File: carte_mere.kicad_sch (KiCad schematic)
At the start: 58 parts, among them J1 Conn_01x02_Pin, J10 Conn_01x03_Pin, J11 Conn_01x03_Pin, J12 Conn_01x03_Pin, J13 Conn_01x03_Pin, J14 Conn_01x03_Pin, J15 Conn_01x03_Pin, J16 Conn_01x03_Pin, J2 Conn_01x03_Pin, J3 Conn_01x03_Pin, J4 Conn_01x03_Pin, J5 Conn_01x03_Pin, J6 Conn_01x03_Pin, J7 Conn_01x03_Pin, J8 Conn_01x03_Pin, J9 Conn_01x03_Pin, U1 SN65HVD230, U2 SN74LVC1T45DBV

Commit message: update schematic
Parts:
- added C1, C2: 22uF, Capacitor_SMD:CP_Elec_5x5.4, symbol Device:CP_Small
- added D3, D4: D_Small, Diode_SMD:D_SMA_Handsoldering, symbol Device:D_Small
- added H1, H2, H3, H4: MountingHole_Pad_MP, MountingHole:MountingHole_3.2mm_M3_DIN965_Pad_TopBottom, symbol Mechanical:MountingHole_Pad_MP
- added J17, J18, J19: Conn_01x05_Pin, symbol Connector:Conn_01x05_Pin
- added J20, J21, J22, J23, J24: Conn_01x02_Pin, symbol Connector:Conn_01x02_Pin
- added R38, R40: 1k, symbol Device:R
- added R39, R41: 2k, symbol Device:R
- added U3: R-78B3.3-2.0, Converter_DCDC:Converter_DCDC_RECOM_R-78B-2.0_THT, symbol Regulator_Switching:R-78B3.3-2.0
- added U4: R-78B5.0-2.0, Converter_DCDC:Converter_DCDC_RECOM_R-78B-2.0_THT, symbol Regulator_Switching:R-78B5.0-2.0
- R10, R14, R20, R22, R27, R30, R5: value 10k -> 1k
- R12, R16, R21, R26, R28, R32, R8: value 10k -> 2k
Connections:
- net +3V3: now also D3.2 (A), U3.3 (OUT)
- net +5V: now also R10.1, R14.1, R20.1, R22.1, R27.1, R30.1, R5.1, D4.2 (A), J17.2 (Pin_2), J18.2 (Pin_2), J19.2 (Pin_2), R38.1, R40.1, U4.3 (OUT); no longer J10.2 (Pin_2), J11.2 (Pin_2), J12.2 (Pin_2), J13.2 (Pin_2), J14.2 (Pin_2), J15.2 (Pin_2), J2.2 (Pin_2), J3.2 (Pin_2), J4.2 (Pin_2), J5.2 (Pin_2), J6.2 (Pin_2), J7.2 (Pin_2), J8.2 (Pin_2), J9.2 (Pin_2), R10.2, R12.2, R14.2, R16.2, R20.2, R21.2, R22.2, R26.2, R27.2, R28.2, R30.2, R32.2, R5.2, R8.2
- net GND: now also R12.2, R16.2, R21.2, R26.2, R28.2, R32.2, R8.2, C1.2, C2.2, H1.MP, H2.MP, H3.MP, H4.MP, J17.5 (Pin_5), J18.5 (Pin_5), J19.5 (Pin_5), J20.2 (Pin_2), J21.2 (Pin_2), J22.2 (Pin_2), J23.2 (Pin_2), J24.2 (Pin_2), R39.2, R41.2, U3.2 (GND), U4.2 (GND)
- net V_AX: now also J24.1 (Pin_1)
- net at J14.3 (Pin_3), R29.2: no longer R30.1
- net at J12.3 (Pin_3), R24.2: no longer R27.1
- net at J3.3 (Pin_3), R7.2: no longer R8.1
- net at J2.3 (Pin_3), R6.2: no longer R5.1
- net at J6.3 (Pin_3), R13.2: no longer R14.1
- net at J8.3 (Pin_3), R17.2: no longer R20.1
- net at J4.3 (Pin_3), R9.2: no longer R10.1
- net at J11.3 (Pin_3), R23.2: no longer R26.1
- net at J15.3 (Pin_3), R31.2: no longer R32.1
- net at J13.3 (Pin_3), R25.2: no longer R28.1
- net at J10.3 (Pin_3), R19.2: no longer R22.1
- net QEI_3_X: now reaches JP1.14 (Y17)
- net QEI_3_X: now also R20.2, R21.1, R30.2, R32.1, J18.4 (Pin_4), J19.4 (Pin_4)
- net QEI_3_B: now reaches JP1.16 (V18)
- net QEI_3_B: now also J19.3 (Pin_3), R38.2, R39.1
- net QEI_3_A: now reaches JP1.18 (Y14)
- net QEI_3_A: now also J19.1 (Pin_1), R40.2, R41.1
- net QEI_1_A: now reaches JP1.23 (V12)
- net QEI_1_A: now also R5.2, R8.1, J17.1 (Pin_1)
- net QEI_1_B: now reaches JP1.25 (T14)
- net QEI_1_B: now also R10.2, R12.1, J17.3 (Pin_3)
- net QEI_1_X: now reaches JP1.27 (T11)
- net QEI_1_X: now also R14.2, R16.1, J17.4 (Pin_4)
- net QEI_2_A: now reaches JP1.31 (V15)
- net QEI_2_A: now also R27.2, R28.1, J18.1 (Pin_1)
- net QEI_2_B: now reaches JP1.33 (P14)
- net QEI_2_B: now also R22.2, R26.1, J18.3 (Pin_3)
- net QEI_2_X: now reaches JP1.35 (U14)
- net at J9.3 (Pin_3), R18.2: no longer R21.1
- net at J7.3 (Pin_3), R15.2: no longer R16.1
- net at J5.3 (Pin_3), R11.2: no longer R12.1
- new net +24V: C1.1, C2.1, D3.1 (K), D4.1 (K), U3.1 (IN), U4.1 (IN)
- new net 5V_POWER: J10.2 (Pin_2), J11.2 (Pin_2), J12.2 (Pin_2), J13.2 (Pin_2), J14.2 (Pin_2), J15.2 (Pin_2), J2.2 (Pin_2), J20.1 (Pin_1), J21.1 (Pin_1), J22.1 (Pin_1), J23.1 (Pin_1), J3.2 (Pin_2), J4.2 (Pin_2), J5.2 (Pin_2), J6.2 (Pin_2), J7.2 (Pin_2), J8.2 (Pin_2), J9.2 (Pin_2)
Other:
- note added: "DC-DC - 3.3V 2A - 5V 2A"
- note added: "Entrée encodeur"
- moved on the sheet: J10, J11, J12, J13, J14, J15, J2, J3, J4, J5, J6, J7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

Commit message: add DSO with current limitation + organisation of the schematic
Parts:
- removed D1, D2: LED, symbol Device:LED
- removed J1: Conn_01x02_Pin, symbol Connector:Conn_01x02_Pin
- removed J10, J11, J12, J13, J14, J15, J16, J2, J3, J4, J5, J6, J7, J8, J9: Conn_01x03_Pin, symbol Connector:Conn_01x03_Pin
- removed J17, J18, J19: Conn_01x05_Pin, symbol Connector:Conn_01x05_Pin
- removed R1, R10, R14, R20, R22, R27, R30, R33, R38, R4, R40, R5: 1k, symbol Device:R
- removed R11, R13, R15, R17, R18, R19, R2, R23, R24, R25, R29, R3, R31, R35, R37, R6, R7, R9: 100R, symbol Device:R
- removed R12, R16, R21, R26, R28, R32, R39, R41, R8: 2k, symbol Device:R
- removed R34: 100k, symbol Device:R
- removed R36: 10k, symbol Device:R
- removed U1: SN65HVD230, Package_SO:SOIC-8_3.9x4.9mm_P1.27mm, symbol Interface_CAN_LIN:SN65HVD230
- removed U2: SN74LVC1T45DBV, Package_TO_SOT_SMD:SOT-23-6, symbol Logic_LevelTranslator:SN74LVC1T45DBV
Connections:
- net DSO_1: now reaches JP1.20 (W16)
- net DSO_2: now reaches JP1.22 (R18)
- net DSO_3: now reaches JP1.24 (W13)
- net DSO_4: now reaches JP1.26 (T15)
- net DSO_5: now reaches JP1.28 (T10)
- net DSO_6: now reaches JP1.32 (W15)
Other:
- added sheet AX12 (AX12.kicad_sch)
- added sheet CAN (CAN.kicad_sch)
- added sheet DSO (DSO.kicad_sch)
- added sheet QEI (QEI.kicad_sch)
- added sheet Servo (Servo.kicad_sch)
- note removed: "AX12"
- note removed: "CAN"
- note removed: "Entrée encodeur"
- note removed: "PWM_SERVO_5V"
- moved on the sheet: C1, C2, D3, D4, J20, J24

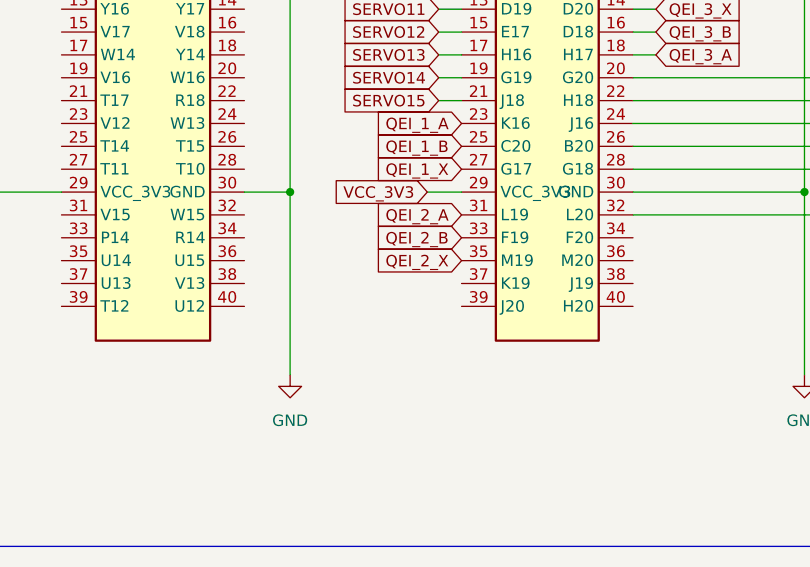
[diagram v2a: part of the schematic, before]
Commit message: update servo output
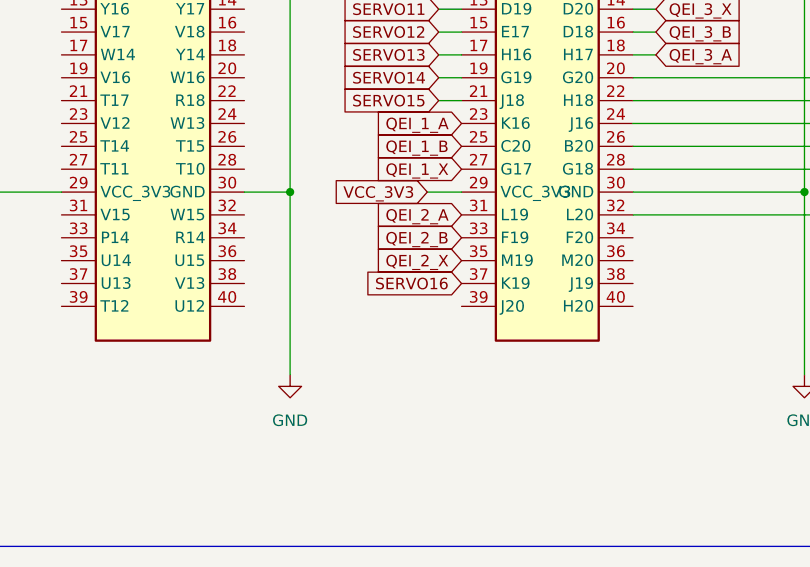
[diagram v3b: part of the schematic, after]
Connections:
- net SERVO16: now reaches JP1.37 (U13)
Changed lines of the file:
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@@
+		)
+	)
+	(global_label "SERVO16"
+		(shape input)
+		(at 82.55 85.09 180)
+		(fields_autoplaced yes)
+		(effects
+			(font
+				(size 1.27 1.27)
+			)
+			(justify right)
+		)
+		(property "Intersheetrefs" "${INTERSHEET_REFS}"
+			(at 71.0982 85.09 0)
+			(effects
+				(font
+					(size 1.27 1.27)
+				)
+				(justify right)
+				(hide yes)
+			)
 		)
 	)

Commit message: update
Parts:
- removed C1, C2: 22uF, Capacitor_SMD:CP_Elec_5x5.4, symbol Device:CP_Small
- removed D3, D4: D_Small, Diode_SMD:D_SMA_Handsoldering, symbol Device:D_Small
- removed J20, J21, J22, J23, J24: Conn_01x02_Pin, symbol Connector:Conn_01x02_Pin
- removed U3: R-78B3.3-2.0, Converter_DCDC:Converter_DCDC_RECOM_R-78B-2.0_THT, symbol Regulator_Switching:R-78B3.3-2.0
- removed U4: R-78B5.0-2.0, Converter_DCDC:Converter_DCDC_RECOM_R-78B-2.0_THT, symbol Regulator_Switching:R-78B5.0-2.0
- added J10: Conn_01x02_Pin, Connector_AMASS:AMASS_XT30U-F_1x02_P5.0mm_Vertical, symbol Connector:Conn_01x02_Pin
- JP1: footprint (none) -> Z7-lite:Z7-lite
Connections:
- net AX_DATA: now also JP1.JP1_5 (T16); no longer JP1.5 (T16)
- net AX_DIR: now also JP1.JP1_7 (W18); no longer JP1.7 (W18)
- net CAND: now also JP1.JP1_3 (R16); no longer JP1.1 (N17)
- net CANR: now also JP1.JP1_1 (N17); no longer JP1.3 (R16)
- net DSO_1: now also JP1.JP2_20 (G20); no longer JP1.20 (W16)
- net DSO_2: now also JP1.JP2_22 (H18); no longer JP1.22 (R18)
- net DSO_3: now also JP1.JP2_24 (J16); no longer JP1.24 (W13)
- net DSO_4: now also JP1.JP2_26 (B20); no longer JP1.26 (T15)
- net DSO_5: now also JP1.JP2_28 (G18); no longer JP1.28 (T10)
- net DSO_6: now also JP1.JP2_32 (L20); no longer JP1.32 (W15)
- net GND: now also JP1.JP1_12 (GND), JP1.JP1_30 (GND), JP1.JP2_12 (GND), JP1.JP2_30 (GND), J10.1 (Pin_1); no longer JP1.12 (GND), JP1.30 (GND)
- net QEI_1_A: now also JP1.JP2_23 (K16); no longer JP1.23 (V12)
- net QEI_1_B: now also JP1.JP2_25 (C20); no longer JP1.25 (T14)
- net QEI_1_X: now also JP1.JP2_27 (G17); no longer JP1.27 (T11)
- net QEI_2_A: now also JP1.JP2_31 (L19); no longer JP1.31 (V15)
- net QEI_2_B: now also JP1.JP2_33 (F19); no longer JP1.33 (P14)
- net QEI_2_X: now also JP1.JP2_35 (M19); no longer JP1.35 (U14)
- net QEI_3_A: now also JP1.JP2_18 (H17); no longer JP1.18 (Y14)
- net QEI_3_B: now also JP1.JP2_16 (D18); no longer JP1.16 (V18)
- net QEI_3_X: now also JP1.JP2_14 (D20); no longer JP1.14 (Y17)
- net SERVO1: now also JP1.JP2_1 (L16); no longer JP1.1 (N17)
- net SERVO10: now also JP1.JP2_10 (A20); no longer JP1.10 (Y19)
- net SERVO11: now also JP1.JP2_13 (D19); no longer JP1.13 (Y16)
- net SERVO12: now also JP1.JP2_15 (E17); no longer JP1.15 (V17)
- net SERVO13: now also JP1.JP2_17 (H16); no longer JP1.17 (W14)
- net SERVO14: now also JP1.JP2_19 (G19); no longer JP1.19 (V16)
- net SERVO15: now also JP1.JP2_21 (J18); no longer JP1.21 (T17)
- net SERVO16: now also JP1.JP2_37 (K19); no longer JP1.37 (U13)
- net SERVO2: now also JP1.JP2_2 (L17); no longer JP1.2 (P18)
- net SERVO3: now also JP1.JP2_3 (H15); no longer JP1.3 (R16)
- net SERVO4: now also JP1.JP2_4 (G15); no longer JP1.4 (R17)
- net SERVO5: now also JP1.JP2_5 (F16); no longer JP1.5 (T16)
- net SERVO6: now also JP1.JP2_6 (F17); no longer JP1.6 (U17)
- net SERVO7: now also JP1.JP2_7 (E18); no longer JP1.7 (W18)
- net SERVO8: now also JP1.JP2_8 (E19); no longer JP1.8 (W19)
- net SERVO9: now also JP1.JP2_9 (B19); no longer JP1.9 (Y18)
- removed net VCC_3V3: JP1.29 (VCC_3V3)
- removed net VCC_5V: JP1.11 (VCC_5V)
- new net 24V: J10.2 (Pin_2)
- new net 3.3V: JP1.JP1_29 (VCC_3V3), JP1.JP2_29 (VCC_3V3)
- new net 5V: JP1.JP1_11 (VCC_5V), JP1.JP2_11 (VCC_5V)
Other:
- added sheet power (power.kicad_sch)
- note removed: "DC-DC - 3.3V 2A - 5V 2A"
- moved on the sheet: H1, H2, H3, H4

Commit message: update schematic + layout
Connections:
- net CAND: now also JP1.JP1_1 (N17); no longer JP1.JP1_3 (R16)
- net CANR: now also JP1.JP1_2 (P18); no longer JP1.JP1_1 (N17)
- net DSO_3: now also JP1.JP2_26 (B20); no longer JP1.JP2_24 (J16)
- net DSO_4: now also JP1.JP2_28 (G18); no longer JP1.JP2_26 (B20)
- net DSO_5: now also JP1.JP2_32 (L20); no longer JP1.JP2_28 (G18)
- net DSO_6: now also JP1.JP2_24 (J16); no longer JP1.JP2_32 (L20)

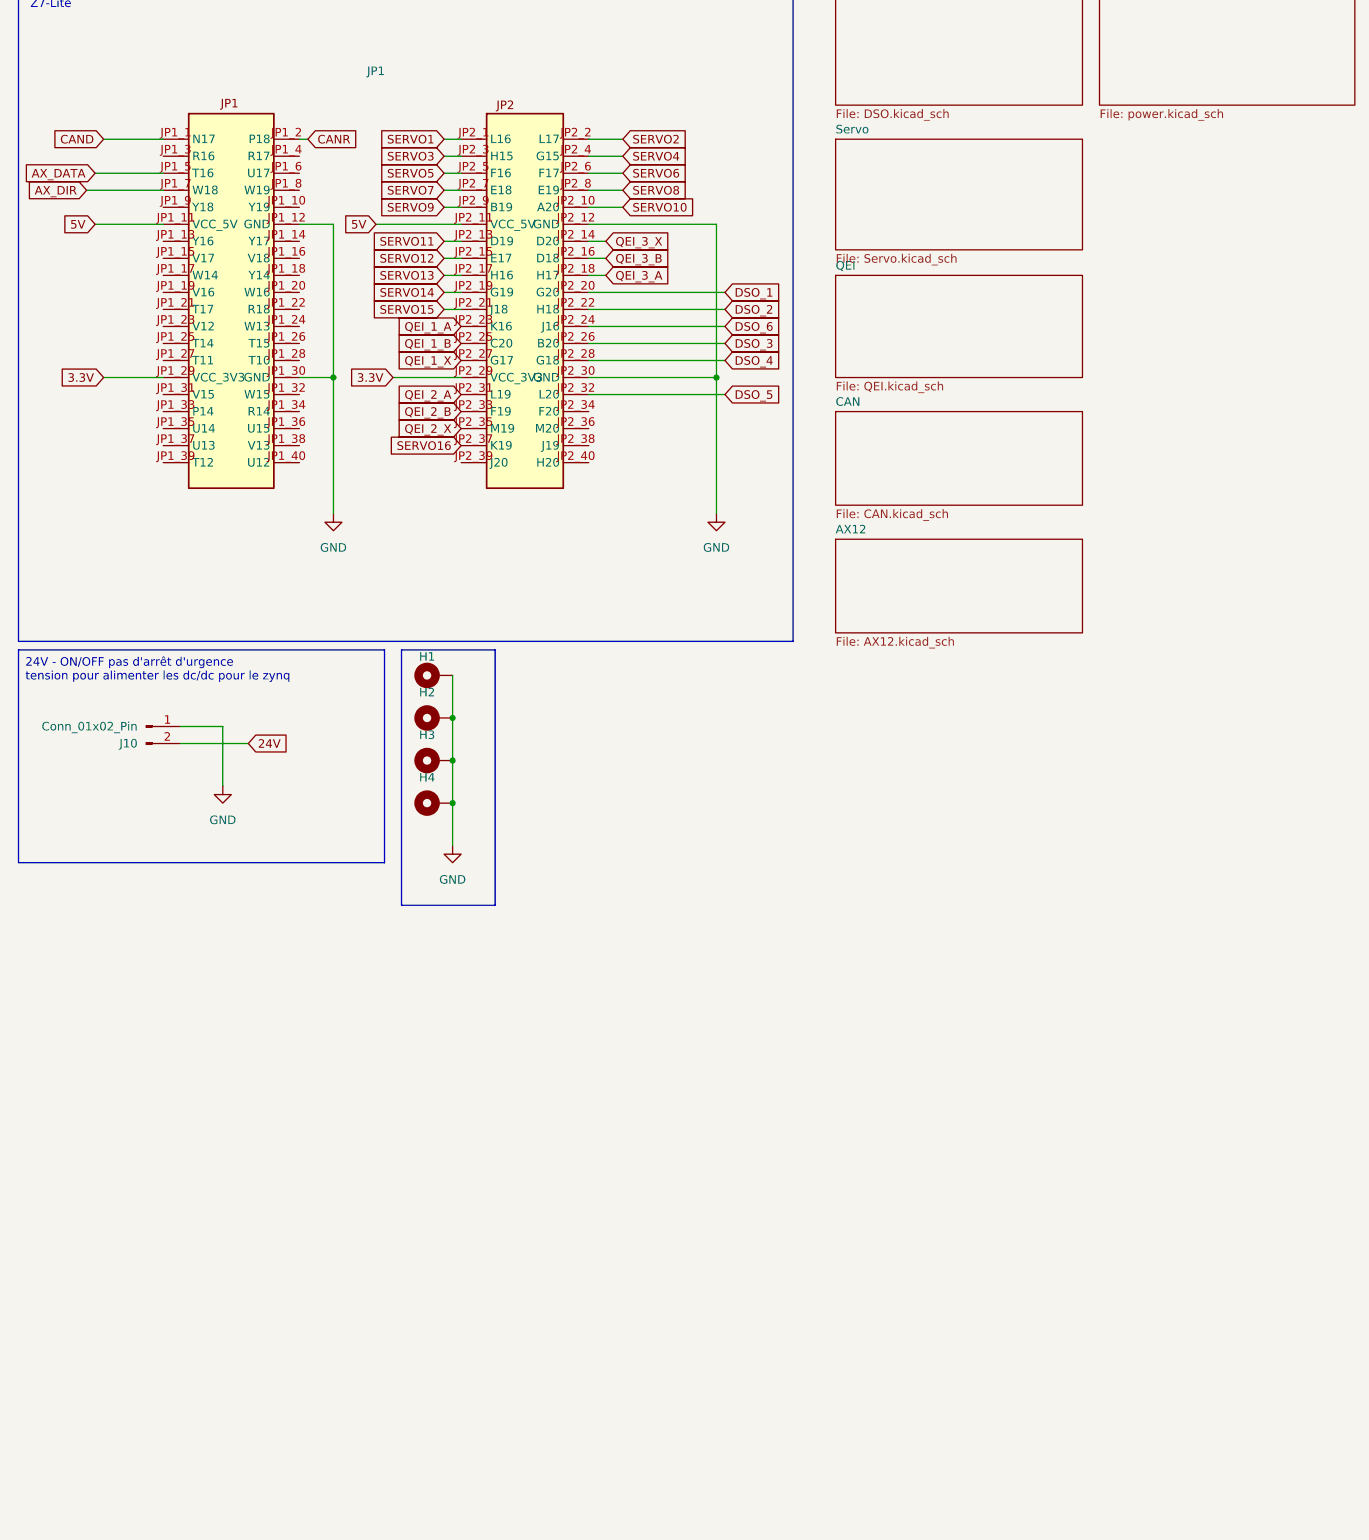
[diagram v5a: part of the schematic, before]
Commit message: v1 - need to change resistor package
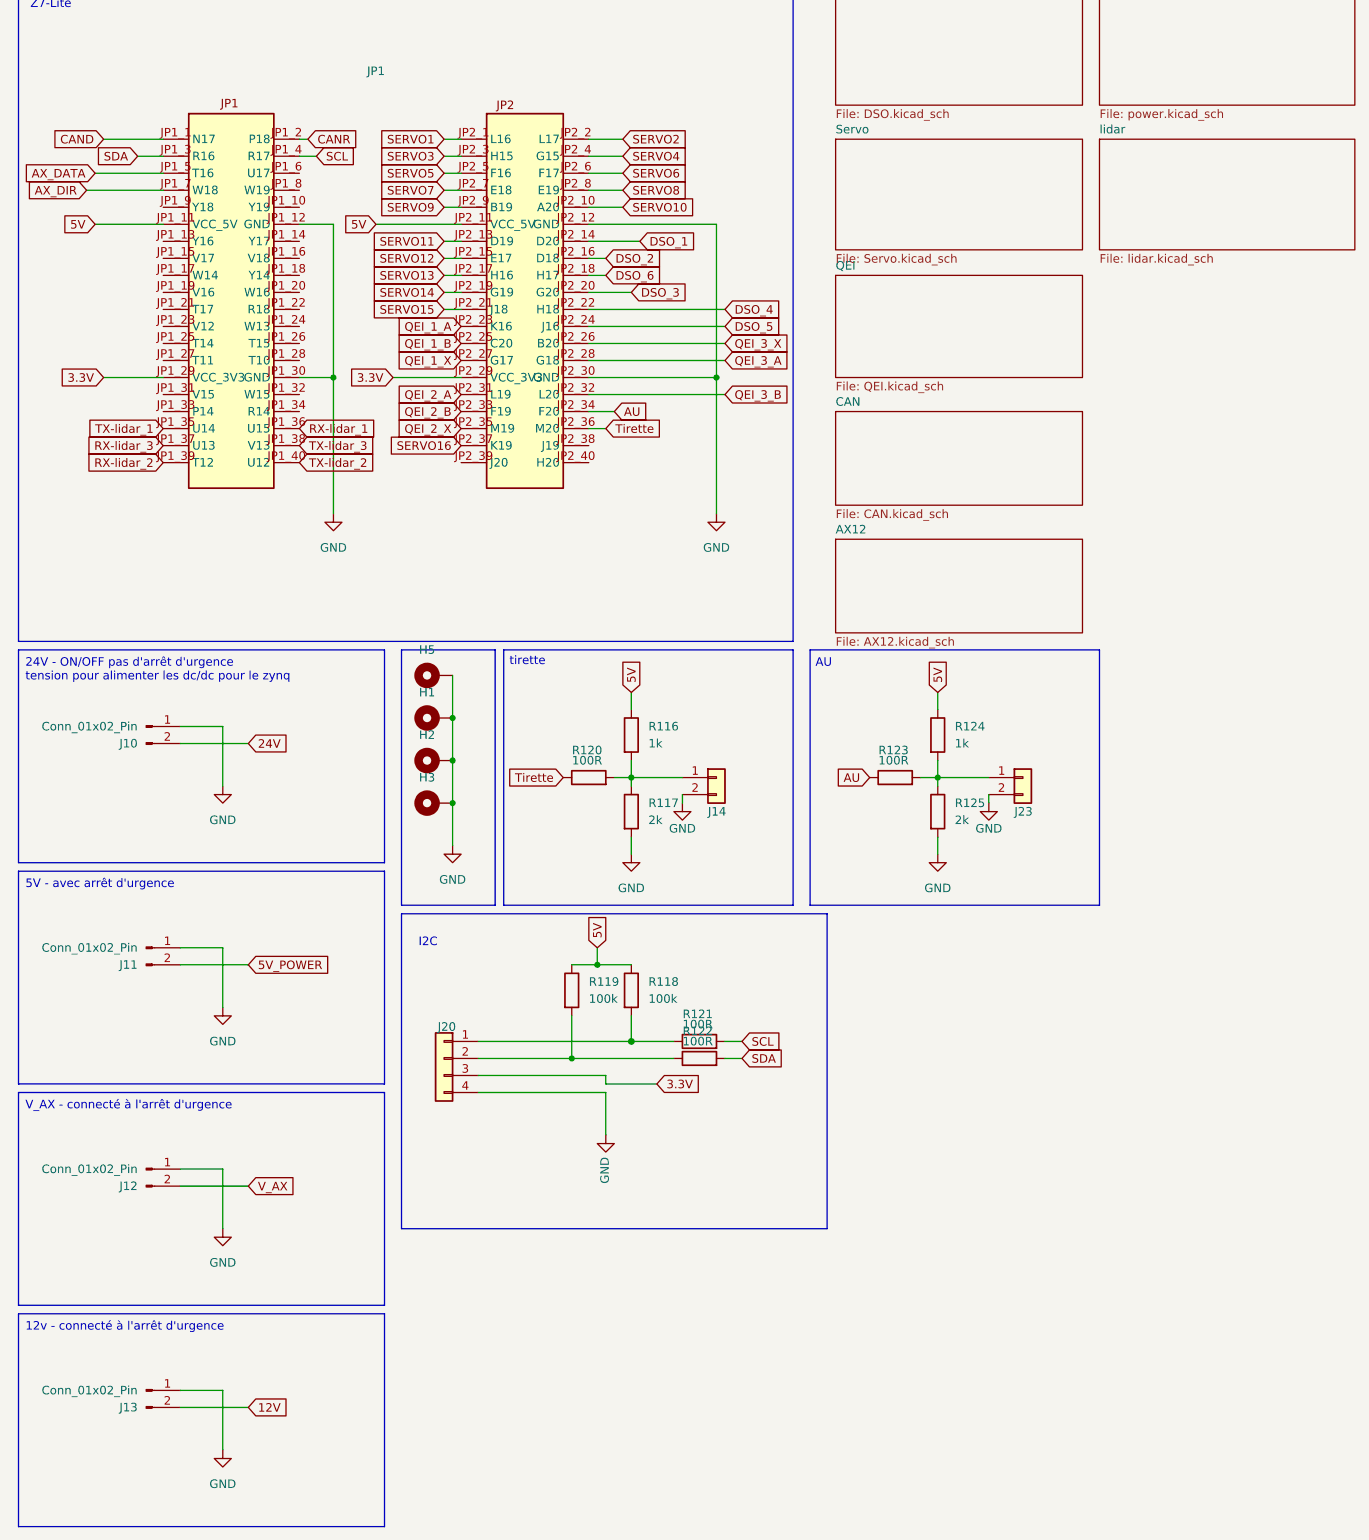
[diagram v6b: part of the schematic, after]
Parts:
- removed H1, H2, H3, H4: MountingHole_Pad_MP, MountingHole:MountingHole_3.2mm_M3_DIN965_Pad_TopBottom, symbol Mechanical:MountingHole_Pad_MP
- added H1, H2, H3, H5: MountingHole_Pad, MountingHole:MountingHole_3.2mm_M3_DIN965_Pad_TopBottom, symbol Mechanical:MountingHole_Pad
- added J11, J12, J13: Conn_01x02_Pin, Connector_AMASS:AMASS_XT30U-F_1x02_P5.0mm_Vertical, symbol Connector:Conn_01x02_Pin
- added J14, J23: Conn_01x02, Connector_Molex:Molex_KK-254_AE-6410-02A_1x02_P2.54mm_Vertical, symbol Connector_Generic:Conn_01x02
- added J20: Conn_01x04, Connector_Molex:Molex_KK-254_AE-6410-04A_1x04_P2.54mm_Vertical, symbol Connector_Generic:Conn_01x04
- added R116, R124: 1k, Capacitor_SMD:C_0402_1005Metric, symbol Device:R
- added R117, R125: 2k, Capacitor_SMD:C_0402_1005Metric, symbol Device:R
- added R118, R119: 100k, Capacitor_SMD:C_0402_1005Metric, symbol Device:R
- added R120, R121, R122, R123: 100R, Capacitor_SMD:C_0402_1005Metric, symbol Device:R
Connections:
- net 3.3V: now also J20.3 (Pin_3)
- net 5V: now also R116.1, R118.1, R119.1, R124.1
- net DSO_1: now also JP1.JP2_14 (D20); no longer JP1.JP2_20 (G20)
- net DSO_2: now also JP1.JP2_16 (D18); no longer JP1.JP2_22 (H18)
- net DSO_3: now also JP1.JP2_20 (G20); no longer JP1.JP2_26 (B20)
- net DSO_4: now also JP1.JP2_22 (H18); no longer JP1.JP2_28 (G18)
- net DSO_5: now also JP1.JP2_24 (J16); no longer JP1.JP2_32 (L20)
- net DSO_6: now also JP1.JP2_18 (H17); no longer JP1.JP2_24 (J16)
- net GND: now also H1.1, H2.1, H3.1, H5.1, J11.1 (Pin_1), J12.1 (Pin_1), J13.1 (Pin_1), J14.2 (Pin_2), J20.4 (Pin_4), J23.2 (Pin_2), R117.2, R125.2
- net QEI_3_A: now also JP1.JP2_28 (G18); no longer JP1.JP2_18 (H17)
- net QEI_3_B: now also JP1.JP2_32 (L20); no longer JP1.JP2_16 (D18)
- net QEI_3_X: now also JP1.JP2_26 (B20); no longer JP1.JP2_14 (D20)
- net SDA: now reaches JP1.JP1_3 (R16)
- net SDA: now also R122.2
- net TX-lidar_1: now reaches JP1.JP1_35 (U14)
- net RX-lidar_1: now reaches JP1.JP1_36 (U15)
- net RX-lidar_3: now reaches JP1.JP1_37 (U13)
- net TX-lidar_3: now reaches JP1.JP1_38 (V13)
- net RX-lidar_2: now reaches JP1.JP1_39 (T12)
- net SCL: now reaches JP1.JP1_4 (R17)
- net SCL: now also R121.2
- net TX-lidar_2: now reaches JP1.JP1_40 (U12)
- net AU: now reaches JP1.JP2_34 (F20)
- net AU: now also R123.1
- net Tirette: now reaches JP1.JP2_36 (M20)
- net Tirette: now also R120.1
- new net: J20.1 (Pin_1), R118.2, R121.1
- new net: J20.2 (Pin_2), R119.2, R122.1
- new net: J23.1 (Pin_1), R123.2, R124.2, R125.1
- new net: J14.1 (Pin_1), R116.2, R117.1, R120.2
- new net 12V: J13.2 (Pin_2)
- new net 5V_POWER: J11.2 (Pin_2)
- new net V_AX: J12.2 (Pin_2)
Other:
- added sheet lidar (lidar.kicad_sch)
- note added: "AU"
- note added: "I2C"
- note added: "tirette"
